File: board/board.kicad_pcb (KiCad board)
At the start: 2 copper layers, 134 parts, among them J202 Conn_01x02, J301 Conn_Coaxial, J401 Conn_Coaxial, J501 Conn_Coaxial, Q201 CPH3350, U101 Pico, U102 CS42438, U201 AZ1117-ADJ, U202 L7805, U203 L7805, U301 lmc6042, U401 lmc6042, U501 lmc6042, U502 HEF4053B, U503 lmc6042

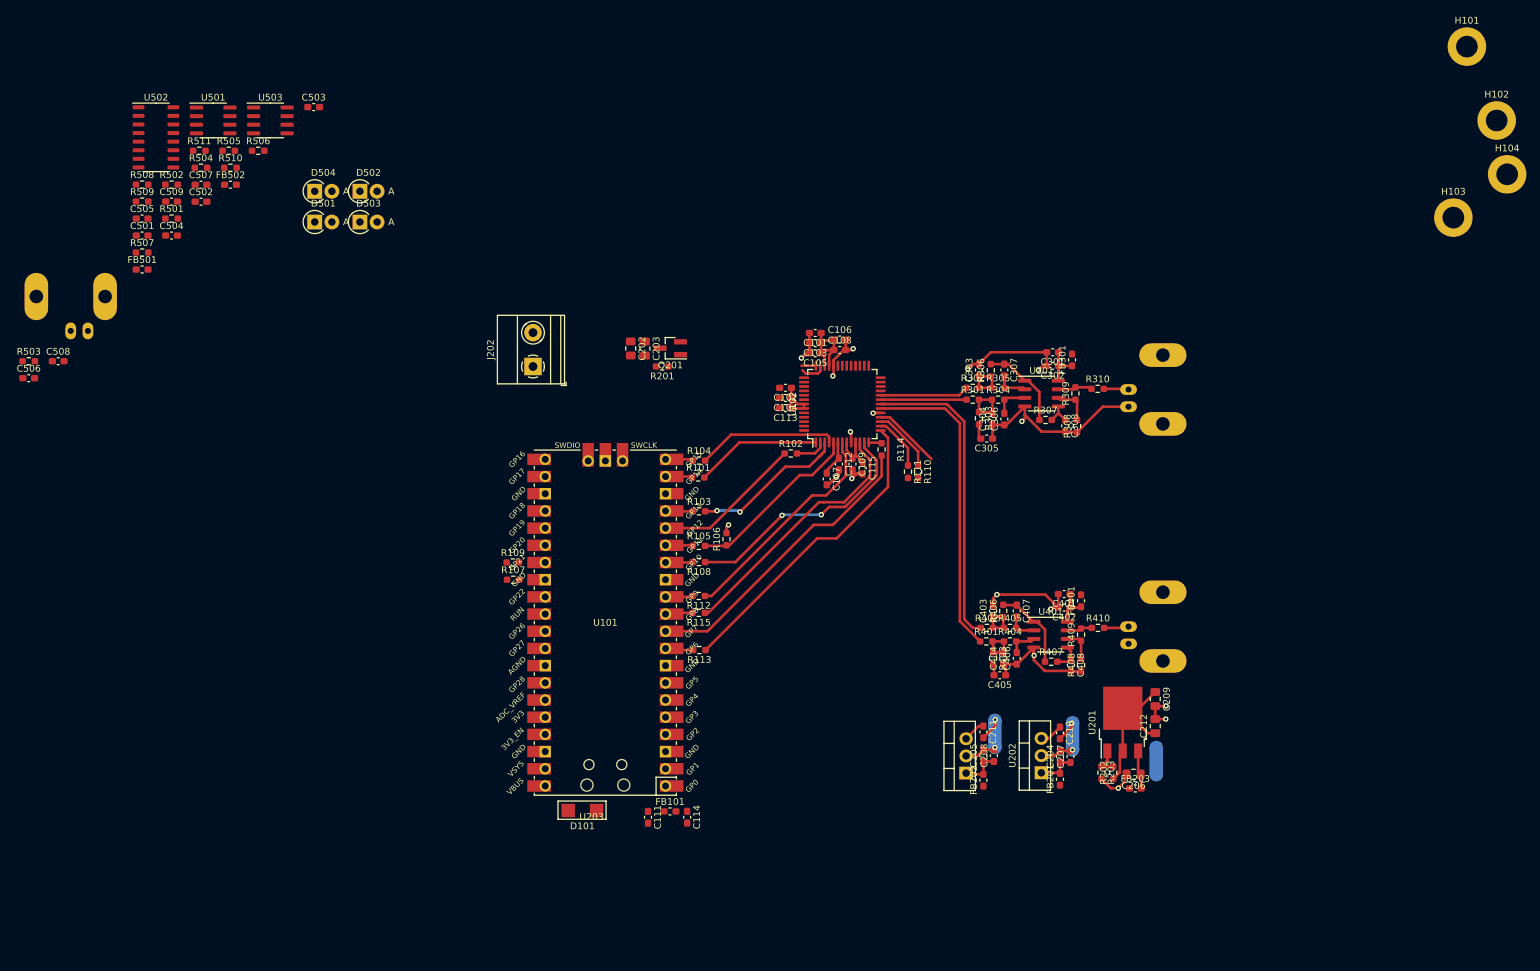
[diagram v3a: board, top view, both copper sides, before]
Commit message: some pcb digital moved
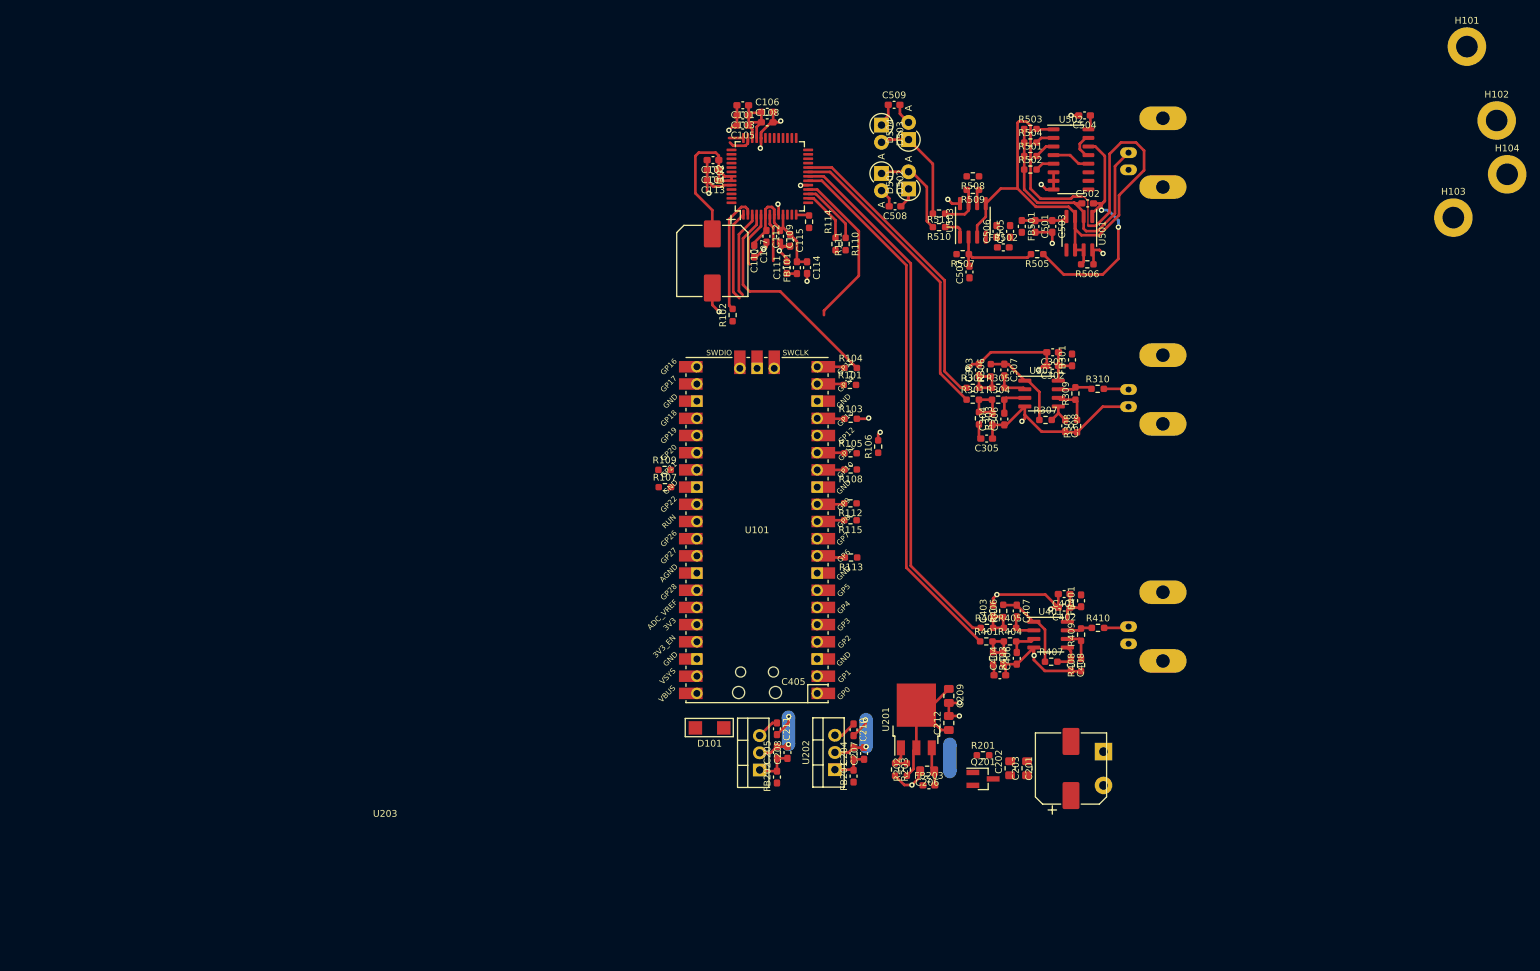
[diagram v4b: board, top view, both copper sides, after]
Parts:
- added C110: 330u, Capacitor_SMD:CP_Elec_10x10, F.Cu at (160.0, 51.5)
- added C201: 330u, Capacitor_SMD:CP_Elec_10x10, F.Cu at (213.0, 126.5)
- C308, C408: value 100n -> 100p
- J202: moved to B.Cu
- moved J501 158.5 mm to (221.5, 35.5), turned to 90 degrees
- moved R503 151.9 mm to (207.0, 32.0)
- moved C506 144.6 mm to (202.0, 47.1), turned to 90 degrees
- moved C504 136.1 mm to (215.0, 30.0), turned to 180 degrees
- moved U502 135.2 mm to (213.0, 36.5)
- moved C501 132.0 mm to (207.7, 46.4), turned to -90 degrees
- moved C502 131.0 mm to (215.5, 43.0)
- moved FB501 130.1 mm to (205.7, 46.4), turned to -90 degrees
- moved U501 129.1 mm to (214.2, 47.4), turned to -90 degrees
- moved C505 128.3 mm to (204.0, 47.1), turned to 90 degrees
- moved R501 127.2 mm to (207.0, 36.0)
- moved R502 126.9 mm to (207.0, 38.0)
- moved C508 125.8 mm to (187.0, 43.4), turned to 180 degrees
- moved R506 123.7 mm to (215.4, 52.0), turned to 180 degrees
- moved R509 122.8 mm to (198.5, 41.0), turned to 180 degrees
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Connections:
- net Net-(C507-Pad2) renamed /a_input/transz_filtered
- net Net-(R507-Pad2) renamed /a_input/vout_n_prer
- net Net-(R508-Pad1) renamed /a_input/single_2_diff_fb
- net Net-(R509-Pad2) renamed /a_input/vout_p_prer
- D501 pad 2: /a_input/VOUT_N -> /AIN_N
- D502 pad 1: /a_input/VOUT_N -> /AIN_N
- D503 pad 2: /a_input/VOUT_P -> /AIN_P
- D504 pad 1: /a_input/VOUT_P -> /AIN_P
- R510 pad 2: /a_input/VOUT_N -> /AIN_N
- R511 pad 2: /a_input/VOUT_P -> /AIN_P
- U102 pad 38: unconnected-(U102-Pad38) -> /AIN_N
- U102 pad 39: unconnected-(U102-Pad39) -> /AIN_P
- U502 pad 1: Net-(U502-Pad1) -> Net-(R503-Pad2)
- U502 pad 12: Net-(R504-Pad2) -> Net-(U502-Pad12)
- U502 pad 13: Net-(R503-Pad2) -> Net-(U502-Pad13)
- U502 pad 14: Net-(U502-Pad14) -> /a_input/transz_out
- U502 pad 15: /a_input/transz_out -> Net-(U502-Pad13)
- U502 pad 2: Net-(U502-Pad14) -> Net-(R504-Pad2)
- U502 pad 4: Net-(U502-Pad1) -> Net-(U502-Pad12)
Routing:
- net /a_input/vbias_buf: track 0.00 -> 104.3 mm
- net /dac_sdin_term: track 45.7 -> 0.00 mm
- net /dac_sdout: track 44.5 -> 0.00 mm
- net /a_input/photo_in: track 0.00 -> 38.4 mm
- net /dac_sclk_term: track 38.4 -> 0.00 mm
- net /a_input/transz_out: track 0.00 -> 36.8 mm, vias 0 -> 2
- net /dac_mclk_term: track 36.3 -> 0.00 mm, vias 2 -> 0
- net GNDA: track 97.7 -> 132.6 mm, vias 12 -> 19
- net /out_1_P: track 45.6 -> 79.3 mm
- net /out_1_N: track 46.1 -> 79.8 mm
- net /out_2_P: track 12.7 -> 45.2 mm
- net /out_2_N: track 13.2 -> 44.8 mm
- net /dac_fs_term: track 33.3 -> 7.04 mm
- net /dac_ctrl_cipo: track 22.2 -> 0.00 mm
- net /AIN_P: track 0.00 -> 18.6 mm
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
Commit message: do the gng
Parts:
- U202, U203: moved to B.Cu
- moved H101 126.8 mm to (202.5, 126.2)
- moved H102 126.8 mm to (206.9, 137.2)
- moved H103 126.8 mm to (200.5, 151.5)
- moved H104 126.8 mm to (208.4, 145.1)
- moved R401 35.7 mm to (224.6, 81.5), turned to -90 degrees
- moved R402 35.5 mm to (226.6, 81.6), turned to -90 degrees
- moved R403 34.6 mm to (222.1, 82.5), turned to 180 degrees
- moved C403 34.6 mm to (229.1, 82.5), turned to 0 degrees
- moved C209 34.5 mm to (214.8, 87.5)
- moved C212 34.5 mm to (214.8, 91.5)
- moved FB203 34.5 mm to (211.8, 100.8)
- moved R202 34.5 mm to (208.6, 98.4)
- moved R203 34.5 mm to (206.8, 98.4)
- moved C204 34.5 mm to (200.7, 96.0)
- moved C206 34.5 mm to (211.6, 98.7)
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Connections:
- C101 pad 1: +5VD -> +5VA
- C102 pad 1: +5VD -> +5VA
- C103 pad 1: +5VD -> +5VA
- C104 pad 1: +5VD -> +5VA
- C105 pad 1: +5VD -> +5VA
- C106 pad 1: +5VD -> /a_input/VBIAS
- C108 pad 1: +5VD -> /a_input/VBIAS
- C110 pad 1: +5VD -> /vfilt
- C113 pad 1: +5VD -> /vfilt
- U102 pad 36: +5VD -> /a_input/VBIAS
- U102 pad 37: +5VD -> +5VA
- U102 pad 38: /AIN_N -> /AIN_P
- U102 pad 39: /AIN_P -> /AIN_N
- U102 pad 46: +5VD -> +5VA
- U102 pad 47: +5VD -> /vfilt
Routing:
- net /AIN_P: track 18.6 -> 57.6 mm
- net /AIN_N: track 17.8 -> 51.3 mm
- net /pico_vin: track 0.00 -> 24.8 mm
- net /dac_ctrl_copi_term: track 33.1 -> 11.4 mm
- net +5VD: track 41.1 -> 20.8 mm
- net /dac_mclk_term: track 0.00 -> 16.9 mm
- net +5VA: track 9.50 -> 26.1 mm
- net /dac_sdin_term: track 0.00 -> 15.4 mm
- net /dac_sclk_term: track 0.00 -> 14.8 mm
- net /a_input/vout_n_prer: track 3.48 -> 16.1 mm
- net /output_stage1/ctrl_output_pre_prot: track 3.76 -> 16.1 mm
- net /vfilt: track 0.00 -> 12.0 mm
- net /dac_sdout: track 0.00 -> 10.3 mm
- net /out_1_P: track 79.3 -> 86.5 mm
- net /dac_aux_sdin_term: track 24.6 -> 18.6 mm
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- added copper zone on F.Cu, net /power/vin
- added copper zone on F.Cu, net /power/vprot
- added copper zone on B.Cu, net GNDA
- added copper zone on F.Cu, net GNDA
- added copper zone on B.Cu, net GNDD
- added copper zone on F.Cu, net GNDD
- added copper zone on B.Cu, net GNDPWR
- added copper zone on F.Cu, net GNDPWR
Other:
- board outline added: 79.4 x 92 mm

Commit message: pcb done
attempt at doing some sw. builds but not tested
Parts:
- moved H103 120.5 mm to (198.0, 31.0)
- moved H102 119.5 mm to (152.0, 31.0)
- moved H101 77.9 mm to (226.0, 52.0)
- moved H104 66.7 mm to (150.0, 113.0)
- moved R106 31.4 mm to (153.4, 83.2), turned to -90 degrees
- moved R104 29.5 mm to (152.8, 77.5), turned to 180 degrees
- moved R101 28.1 mm to (152.7, 74.8), turned to 180 degrees
- moved R105 27.5 mm to (152.9, 79.9), turned to 180 degrees
- moved R103 27.0 mm to (153.9, 69.9), turned to -90 degrees
- moved R113 26.8 mm to (179.4, 68.6), turned to -90 degrees
- moved R109 21.9 mm to (180.5, 92.5)
- moved R107 21.5 mm to (179.5, 95.5), turned to -90 degrees
- moved R108 19.6 mm to (176.5, 63.1), turned to -90 degrees
- moved R115 12.3 mm to (180.4, 77.5)
- moved D101 7.35 mm to (180.9, 103.2)
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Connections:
- net Net-(U502-Pad12) renamed /a_input/transz_x1
- net Net-(U502-Pad13) renamed /a_input/transz_x2
- H101 pad 1: GNDPWR -> GNDA
- H102 pad 1: GNDPWR -> GNDA
- H103 pad 1: GNDPWR -> GNDA
- H104 pad 1: GNDPWR -> GNDD
- R106 pad 1: /dac_ctrl_rstn_term -> /dac_ctrl_rstn
- U101 pad 1: unconnected-(U101-Pad1) -> /transz_rf3
- U101 pad 10: /dac_sdout -> /dac_aux_sdin
- U101 pad 11: /dac_sclk -> /dac_aux_sclk
- U101 pad 12: /dac_fs -> /dac_aux_lrck
- U101 pad 14: /dac_mclk -> unconnected-(U101-Pad14)
- U101 pad 15: /dac_ctrl_rstn -> /dac_fs
- U101 pad 16: /dac_ctrl_cipo -> /dac_sclk
- U101 pad 17: /dac_ctrl_csn -> /dac_sdout
- U101 pad 19: /dac_ctrl_clk -> /dac_sdin
- U101 pad 2: unconnected-(U101-Pad2) -> /transz_rf2
- U101 pad 20: /dac_ctrl_copi -> /dac_mclk
- U101 pad 21: unconnected-(U101-Pad21) -> /dac_ctrl_cipo
- U101 pad 22: unconnected-(U101-Pad22) -> /dac_ctrl_csn
- U101 pad 24: unconnected-(U101-Pad24) -> /dac_ctrl_clk
- U101 pad 25: /dac_aux_lrck -> /dac_ctrl_copi
- U101 pad 26: /dac_aux_sclk -> /dac_ctrl_rstn
- U101 pad 27: /dac_aux_sdin -> unconnected-(U101-Pad27)
- U101 pad 4: unconnected-(U101-Pad4) -> /transz_rf1
- U101 pad 9: /dac_sdin -> unconnected-(U101-Pad9)
- U502 pad 10: /a_input/TRANSZ_RF_SW2 -> /transz_rf2
- U502 pad 11: /a_input/TRANSZ_RF_SW1 -> /transz_rf1
- U502 pad 9: /a_input/TRANSZ_RF_SW3 -> /transz_rf3
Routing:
- net +5VA: track 26.1 -> 301.1 mm, vias 0 -> 4
- net /transz_rf3: track 0.00 -> 182.7 mm, vias 0 -> 2
- net VDDA: track 25.3 -> 206.0 mm
- net /transz_rf2: track 0.00 -> 175.9 mm, vias 0 -> 2
- net /transz_rf1: track 0.00 -> 170.2 mm, vias 0 -> 2
- net /a_input/VBIAS: track 4.16 -> 66.3 mm, vias 0 -> 2
- net /dac_aux_lrck: track 0.00 -> 46.5 mm
- net /dac_aux_sclk: track 3.59 -> 49.3 mm
- net /dac_aux_sdin_term: track 18.6 -> 62.7 mm
- net /dac_ctrl_rstn_term: track 12.1 -> 44.9 mm
- net /dac_fs_term: track 12.0 -> 43.9 mm
- net /dac_ctrl_copi_term: track 11.4 -> 42.2 mm
- net GNDD: track 23.1 -> 52.4 mm, vias 7 -> 11
- net /dac_sclk_term: track 14.8 -> 42.8 mm
- net /pico_3v3_out: track 4.97 -> 29.9 mm, vias 0 -> 2
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- added copper zone on B.Cu, net /pico_3v3_out
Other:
- board size 79.4 x 92 mm -> 88.2 x 92 mm
- board text added: "."
- board text added: "Anton Lööf 2022"
- board text added: "Piezo ctrl"
- board text added: "in"
- board text added: "out1"
- board text added: "out2"
- board text added: "vin gnd"

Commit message: Order pcb
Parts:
- C101, C102, C103, C104, C105, C106, C107, C108, C109, C111, C112, C113, C114, C115, C301, C302, C401, C402, C501, C503, C504, C505, C506, FB101, FB301, FB401, FB501, FB502: moved to B.Cu
- moved H103 54.5 mm to (191.0, 85.0)
- moved C504 23.5 mm to (206.6, 51.9), turned to 90 degrees
- moved R503 23.3 mm to (217.6, 52.8), turned to 180 degrees
- moved R504 19.9 mm to (217.6, 50.8), turned to 180 degrees
- moved R506 19.8 mm to (214.0, 32.2), turned to -90 degrees
- moved FB501 17.1 mm to (215.0, 37.8), turned to 90 degrees
- moved R501 16.6 mm to (217.6, 48.8), turned to 180 degrees
- moved FB502 13.8 mm to (203.9, 37.3)
- moved R502 13.8 mm to (217.6, 46.8), turned to 180 degrees
- moved C110 12.8 mm to (153.5, 40.5)
- moved U502 11.9 mm to (211.6, 48.3), turned to 180 degrees
- moved C506 11.2 mm to (207.4, 37.3)
- moved C507 11.0 mm to (205.4, 44.9)
- moved R507 11.0 mm to (204.4, 42.3)
- moved R509 11.0 mm to (205.9, 32.8)
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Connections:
- H103 pad 1: GNDA -> GNDD
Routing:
- net GNDA: track 132.0 -> 48.5 mm, vias 19 -> 25
- net GNDD: track 52.4 -> 8.78 mm, vias 11 -> 8
- net /transz_rf3: track 182.7 -> 149.1 mm, vias 2 -> 1
- net /pico_3v3_out: track 29.9 -> 0.00 mm, vias 2 -> 0
- net /transz_rf2: track 175.9 -> 146.4 mm, vias 2 -> 1
- net /transz_rf1: track 170.2 -> 145.0 mm, vias 2 -> 1
- net /a_input/vbias_buf: track 104.4 -> 81.7 mm
- net /a_input/transz_out: track 36.8 -> 14.6 mm, vias 2 -> 0
- net VDDA: track 206.0 -> 223.3 mm, vias 0 -> 4
- net +5VA: track 301.1 -> 284.3 mm, vias 4 -> 5
- net /a_input/photo_in: track 38.4 -> 27.8 mm
- net /output_stage1/ctrl_output_pre_prot: track 18.4 -> 9.03 mm
- net /AIN_N: track 53.7 -> 44.5 mm
- net /AIN_P: track 57.9 -> 49.9 mm
- net /a_input/vdda_filt_tranz: track 11.7 -> 4.81 mm, vias 0 -> 1
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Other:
- board text added: "GND"
- board text added: "IN"
- board text added: "JLCJLCJLCJLC"
- board text added: "OUT1"
- board text added: "OUT2"
- board text added: "PIEZO CONTROLLER ANTON LÖÖF 2022"
- board text added: "VIN"
- board text removed: "."
- board text removed: "Anton Lööf 2022"
- board text removed: "Piezo ctrl"
- board text removed: "in"
- board text removed: "out1"
- board text removed: "out2"
- board text removed: "vin gnd"

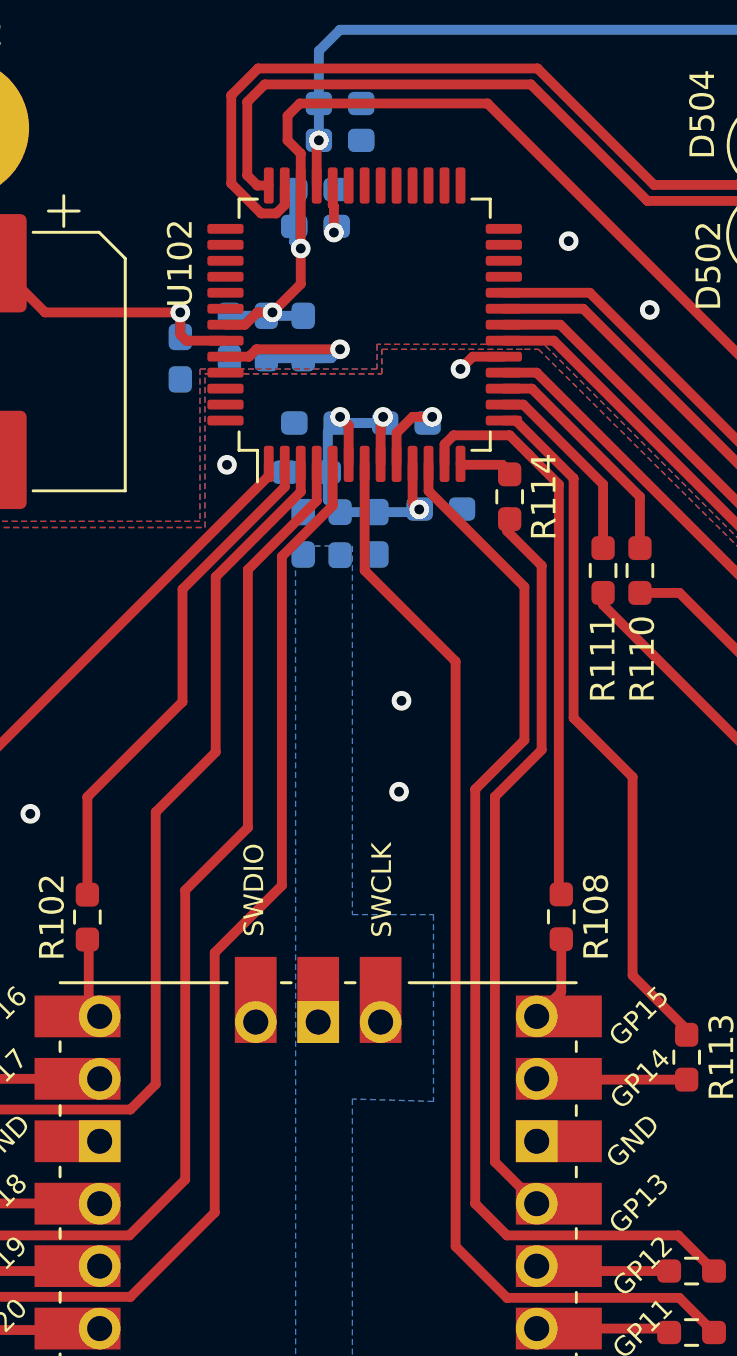
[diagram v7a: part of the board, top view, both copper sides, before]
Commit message: add proper footprint for codec
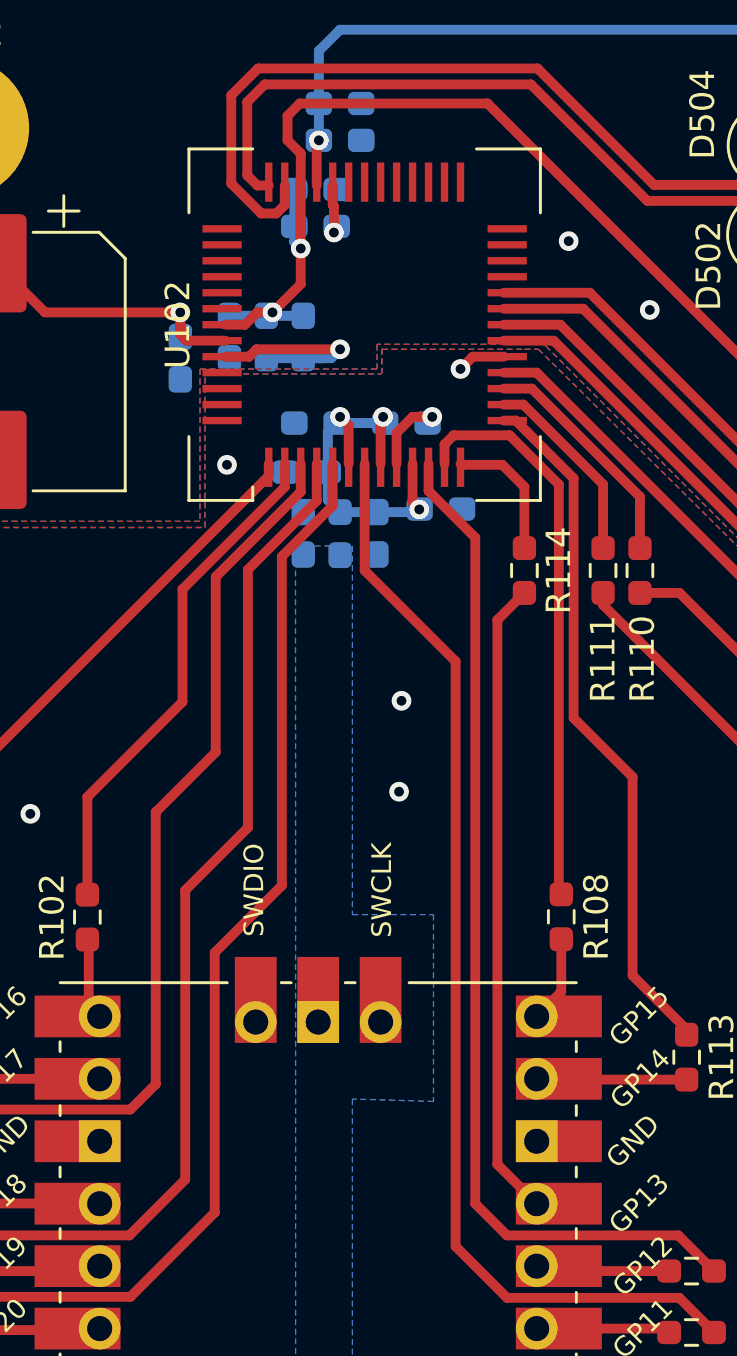
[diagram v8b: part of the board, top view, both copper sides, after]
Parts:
- U102: footprint Package_QFP:LQFP-52_10x10mm_P0.65mm -> good_things:QFP-52_14x14_Pitch0.65mm
- moved R114 3.06 mm to (175.0, 49.0)
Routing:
- net /dac_sdout: track 30.2 -> 26.0 mm
- net /dac_sdout_term: track 2.23 -> 5.48 mm
- net /dac_sclk_term: track 43.4 -> 41.7 mm
